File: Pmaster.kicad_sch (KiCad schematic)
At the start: 158 parts, among them U1 Pico, U2 Pico, U3 LM4040LP-3, U4 Pico, U5 Pico

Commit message: First try to fit electronic on PCB
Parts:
- NT294: renamed from NT291; symbol Device:NetTie_2 -> Analog_ADC:INA219AxDCN
- R15: renamed from R24; symbol Device:R_US -> Analog_ADC:INA219AxDCN
- TP26: renamed from TP29; footprint Connector_Pin:Pin_D1.2mm_L11.3mm_W3.0mm_Flat -> Connector_Pin:Pin_D1.0mm_L10.0mm
- TP27: renamed from TP30; footprint Connector_Pin:Pin_D1.2mm_L11.3mm_W3.0mm_Flat -> Connector_Pin:Pin_D1.0mm_L10.0mm
- TP28: renamed from TP31; footprint Connector_Pin:Pin_D1.2mm_L11.3mm_W3.0mm_Flat -> Connector_Pin:Pin_D1.0mm_L10.0mm
- TP29: renamed from TP32; footprint Connector_Pin:Pin_D1.2mm_L11.3mm_W3.0mm_Flat -> Connector_Pin:Pin_D1.0mm_L10.0mm
- TP30: renamed from TP33; footprint Connector_Pin:Pin_D1.2mm_L11.3mm_W3.0mm_Flat -> Connector_Pin:Pin_D1.0mm_L10.0mm
- TP31: renamed from TP34; footprint Connector_Pin:Pin_D1.2mm_L11.3mm_W3.0mm_Flat -> Connector_Pin:Pin_D1.0mm_L10.0mm
- TP32: renamed from TP35; footprint Connector_Pin:Pin_D1.2mm_L11.3mm_W3.0mm_Flat -> Connector_Pin:Pin_D1.0mm_L10.0mm
- TP33: renamed from TP36; footprint Connector_Pin:Pin_D1.2mm_L11.3mm_W3.0mm_Flat -> Connector_Pin:Pin_D1.0mm_L10.0mm
- TP34: renamed from TP37; footprint Connector_Pin:Pin_D1.2mm_L11.3mm_W3.0mm_Flat -> Connector_Pin:Pin_D1.0mm_L10.0mm
- TP35: renamed from TP38; footprint Connector_Pin:Pin_D1.2mm_L11.3mm_W3.0mm_Flat -> Connector_Pin:Pin_D1.0mm_L10.0mm
- TP36: renamed from TP39; footprint Connector_Pin:Pin_D1.2mm_L11.3mm_W3.0mm_Flat -> Connector_Pin:Pin_D1.0mm_L10.0mm
- TP37: renamed from TP40; footprint Connector_Pin:Pin_D1.2mm_L11.3mm_W3.0mm_Flat -> Connector_Pin:Pin_D1.0mm_L10.0mm
- TP38: renamed from TP41; footprint Connector_Pin:Pin_D1.2mm_L11.3mm_W3.0mm_Flat -> Connector_Pin:Pin_D1.0mm_L10.0mm
- TP39: renamed from TP42; footprint Connector_Pin:Pin_D1.2mm_L11.3mm_W3.0mm_Flat -> Connector_Pin:Pin_D1.0mm_L10.0mm
- TP40: renamed from TP43; footprint Connector_Pin:Pin_D1.2mm_L11.3mm_W3.0mm_Flat -> Connector_Pin:Pin_D1.0mm_L10.0mm
- TP41: renamed from TP44; footprint Connector_Pin:Pin_D1.2mm_L11.3mm_W3.0mm_Flat -> Connector_Pin:Pin_D1.0mm_L10.0mm
- TP42: renamed from TP45; footprint Connector_Pin:Pin_D1.2mm_L11.3mm_W3.0mm_Flat -> Connector_Pin:Pin_D1.0mm_L10.0mm
- TP43: renamed from TP46; footprint Connector_Pin:Pin_D1.2mm_L11.3mm_W3.0mm_Flat -> Connector_Pin:Pin_D1.0mm_L10.0mm
- TP44: renamed from TP47; footprint Connector_Pin:Pin_D1.2mm_L11.3mm_W3.0mm_Flat -> Connector_Pin:Pin_D1.0mm_L10.0mm
- TP45: renamed from TP48; footprint Connector_Pin:Pin_D1.2mm_L11.3mm_W3.0mm_Flat -> Connector_Pin:Pin_D1.0mm_L10.0mm
- TP46: renamed from TP49; footprint Connector_Pin:Pin_D1.2mm_L11.3mm_W3.0mm_Flat -> Connector_Pin:Pin_D1.0mm_L10.0mm
- TP47: renamed from TP50; footprint Connector_Pin:Pin_D1.2mm_L11.3mm_W3.0mm_Flat -> Connector_Pin:Pin_D1.0mm_L10.0mm
- TP48: renamed from TP51; footprint Connector_Pin:Pin_D1.2mm_L11.3mm_W3.0mm_Flat -> Connector_Pin:Pin_D1.0mm_L10.0mm
- TP49: renamed from TP52; footprint Connector_Pin:Pin_D1.2mm_L11.3mm_W3.0mm_Flat -> Connector_Pin:Pin_D1.0mm_L10.0mm
- TP50: renamed from TP53; footprint Connector_Pin:Pin_D1.2mm_L11.3mm_W3.0mm_Flat -> Connector_Pin:Pin_D1.0mm_L10.0mm
- TP51: renamed from TP54; footprint Connector_Pin:Pin_D1.2mm_L11.3mm_W3.0mm_Flat -> Connector_Pin:Pin_D1.0mm_L10.0mm
- TP52: renamed from TP55; footprint Connector_Pin:Pin_D1.2mm_L11.3mm_W3.0mm_Flat -> Connector_Pin:Pin_D1.0mm_L10.0mm
- TP53: renamed from TP56; footprint Connector_Pin:Pin_D1.2mm_L11.3mm_W3.0mm_Flat -> Connector_Pin:Pin_D1.0mm_L10.0mm
- TP54: renamed from TP57; footprint Connector_Pin:Pin_D1.2mm_L11.3mm_W3.0mm_Flat -> Connector_Pin:Pin_D1.0mm_L10.0mm
- renumbered NT230 to NT233, NT231 to NT234, NT232 to NT235, NT233 to NT236, NT234 to NT237, NT235 to NT238, NT236 to NT239, NT237 to NT240, NT238 to NT241, NT239 to NT242, NT240 to NT243, NT241 to NT244, NT242 to NT245, NT243 to NT246, NT244 to NT247, NT245 to NT248, NT246 to NT249, NT247 to NT250, NT248 to NT251, NT249 to NT252, NT250 to NT253, NT251 to NT254, NT252 to NT255, NT253 to NT256, NT254 to NT257, NT255 to NT258, NT256 to NT259, NT257 to NT260, NT258 to NT261, NT259 to NT262, NT260 to NT263, NT261 to NT264, NT262 to NT265, NT263 to NT266, NT264 to NT267, NT265 to NT268, NT266 to NT269, NT267 to NT270, NT268 to NT271, NT269 to NT272, NT270 to NT273, NT271 to NT274, NT272 to NT275, NT273 to NT276, NT274 to NT277, NT275 to NT278, NT276 to NT279, NT277 to NT280, NT278 to NT281, NT279 to NT282, NT280 to NT283, NT281 to NT284, NT282 to NT285, NT283 to NT286, NT284 to NT287, NT285 to NT288, NT286 to NT289, NT287 to NT290, NT288 to NT291, NT289 to NT292, NT290 to NT293, NT292 to NT295, NT293 to NT296, NT294 to NT297, NT295 to NT298, NT296 to NT299, NT297 to NT300, NT298 to NT301, NT299 to NT302, NT300 to NT303, NT301 to NT304, NT302 to NT305, NT303 to NT306, NT304 to NT307, NT305 to NT308, NT306 to NT309, NT307 to NT310, NT308 to NT311, NT309 to NT312, NT310 to NT313, NT311 to NT314, NT312 to NT315, NT313 to NT316, NT314 to NT317, NT315 to NT318, NT316 to NT319, NT317 to NT320, NT318 to NT321, NT319 to NT322, NT320 to NT323, NT321 to NT324, NT322 to NT325, NT323 to NT326, NT324 to NT327, NT325 to NT328, NT326 to NT329, NT327 to NT330, NT328 to NT331, NT329 to NT332, NT330 to NT333, NT331 to NT334, NT332 to NT335, NT333 to NT336, NT334 to NT337, NT335 to NT338, NT336 to NT339, NT337 to NT340, NT338 to NT341, NT339 to NT342, NT340 to NT343, NT341 to NT344, NT342 to NT345, NT343 to NT346, NT344 to NT347, NT345 to NT348, R19 to R10, R20 to R11, R21 to R12, R22 to R13, R23 to R14, R25 to R16, R26 to R17, U4 to U3, U5 to U4, U3 to U5
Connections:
- net B31_D: no longer NT294.1
- net GND: no longer R15.1
- net S2_I2C_ID1: no longer R15.2
- net at U4.2 (GPIO1): no longer NT294.2

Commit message: backup 1 bank done
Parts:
- removed NT294: S3_01, NetTie:NetTie-2_THT_Pad1.0mm, symbol Analog_ADC:INA219AxDCN
- removed R15: 4.7K, Resistor_THT:R_Axial_DIN0309_L9.0mm_D3.2mm_P12.70mm_Horizontal, symbol Analog_ADC:INA219AxDCN
- added NT294: S3_01, NetTie:NetTie-2_Front1.0mm, symbol Device:NetTie_2
- added R1: 4.7K, Resistor_THT:R_Axial_DIN0309_L9.0mm_D3.2mm_P12.70mm_Horizontal, symbol Device:R_US
- NT233, NT234, NT235, NT236, NT237, NT238, NT239, NT240, NT241, NT242, NT243, NT244, NT245, NT246, NT247, NT248, NT249, NT250, NT251, NT252, NT253, NT254, NT255, NT256, NT257, NT258, NT259, NT260, NT261, NT262, NT263, NT264, NT265, NT266, NT267, NT268, NT269, NT270, NT271, NT272, NT273, NT274, NT275, NT276, NT277, NT278, NT279, NT280, NT281, NT282, NT283, NT284, NT285, NT286, NT287, NT288, NT289, NT290, NT291, NT292, NT293, NT295, NT296, NT297, NT298, NT299, NT300, NT301, NT302, NT303, NT304, NT305, NT306, NT307, NT308, NT309, NT310, NT311, NT312, NT313, NT314, NT315, NT316, NT317, NT318, NT319, NT320, NT321, NT322, NT323, NT324, NT325, NT326, NT327, NT328, NT329, NT330, NT331, NT332, NT333, NT334, NT335, NT336, NT337, NT338, NT339, NT340, NT341, NT342, NT343, NT344, NT345, NT346, NT347, NT348: footprint NetTie:NetTie-2_THT_Pad1.0mm -> NetTie:NetTie-2_Front1.0mm
- TP26, TP27, TP28, TP29, TP30, TP31, TP32, TP33, TP34, TP35, TP36, TP37, TP38, TP39, TP40, TP41, TP42, TP43, TP44, TP45, TP46, TP47, TP48, TP49, TP50, TP51, TP52, TP53, TP54: footprint Connector_Pin:Pin_D1.0mm_L10.0mm -> Connector_Pin:Pin_D0.9mm_L10.0mm_W2.4mm_FlatFork
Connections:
- net B31_D: now also NT294.1
- net GND: now also R1.1
- net S2_I2C_ID1: now also R1.2
- net at U4.2 (GPIO1): now also NT294.2

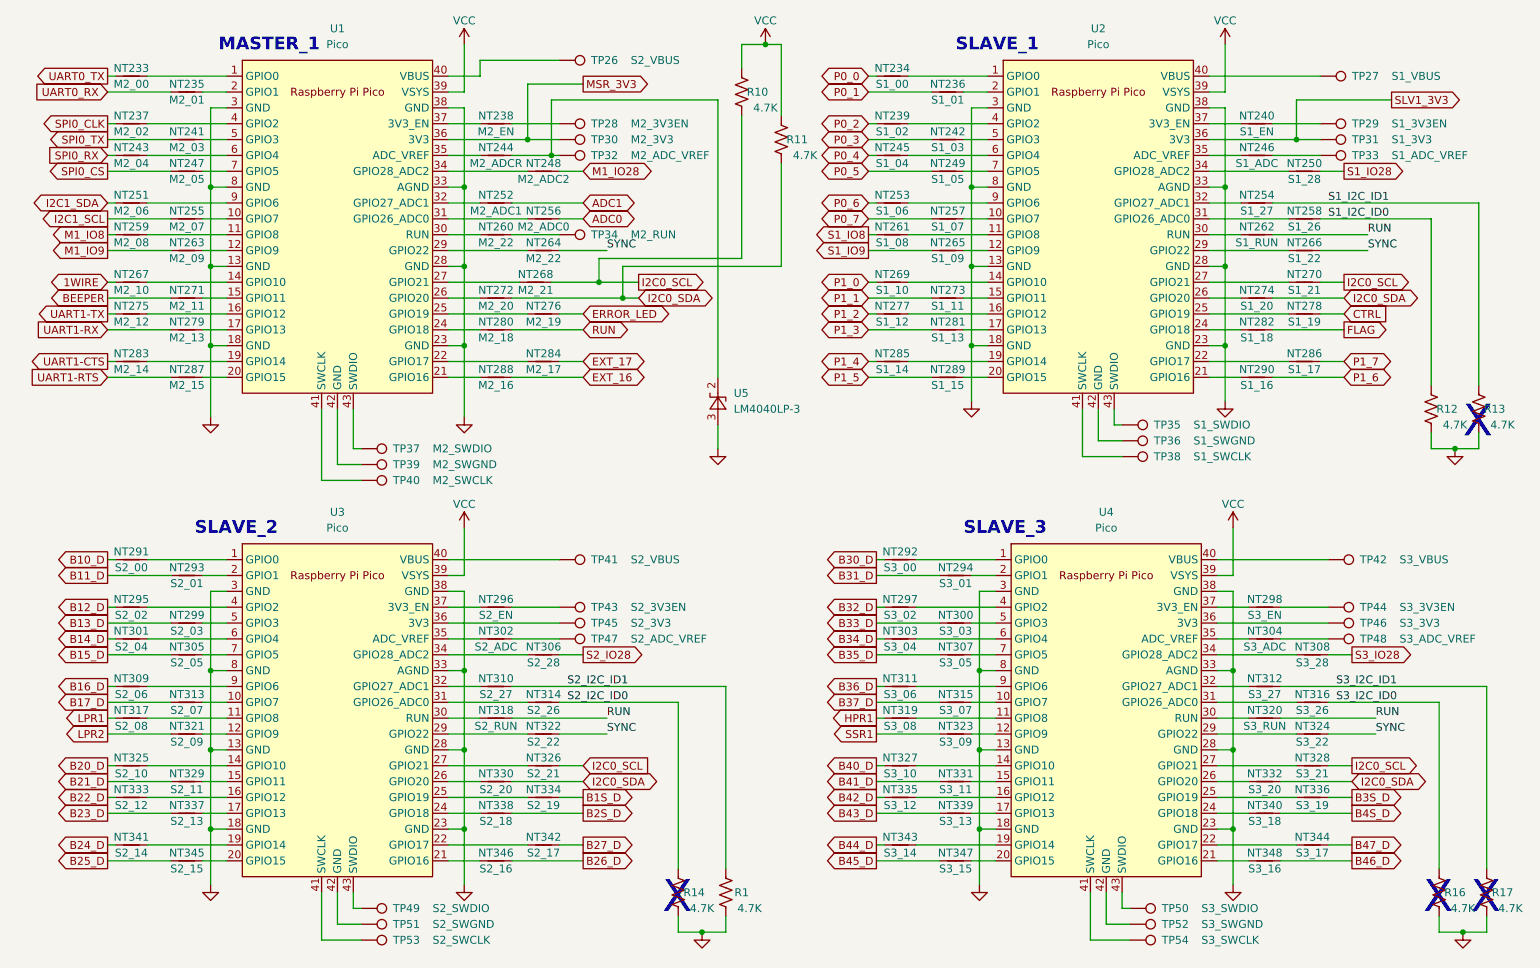
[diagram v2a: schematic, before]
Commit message: half PCB completed
FTS io controller PCB
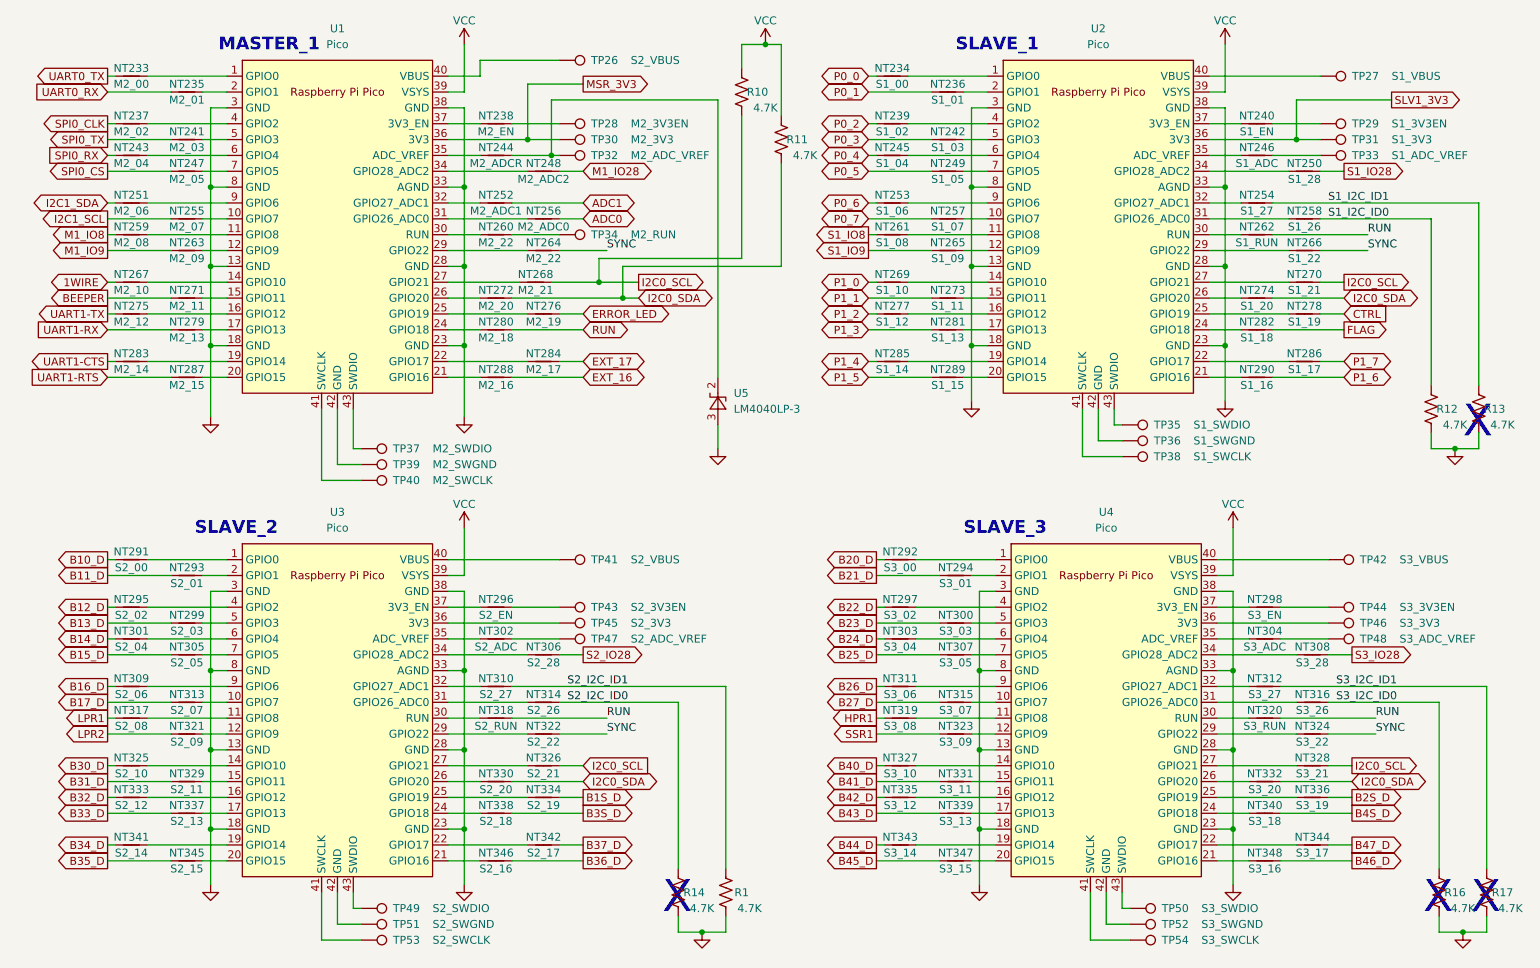
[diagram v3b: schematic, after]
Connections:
- net B20_D: now also NT292.1; no longer NT325.1
- net B21_D: now also NT294.1; no longer NT329.1
- net B22_D: now also NT297.1; no longer NT333.1
- net B23_D: now also NT300.1; no longer NT337.1
- net B24_D: now also NT303.1; no longer NT341.1
- net B25_D: now also NT307.1; no longer NT345.1
- net B26_D: now also NT311.1; no longer NT346.1
- net B27_D: now also NT315.1; no longer NT342.1
- net B2S_D: now also NT336.1; no longer NT338.1
- net B30_D: now also NT325.1; no longer NT292.1
- net B31_D: now also NT329.1; no longer NT294.1
- net B32_D: now also NT333.1; no longer NT297.1
- net B33_D: now also NT337.1; no longer NT300.1
- net B34_D: now also NT341.1; no longer NT303.1
- net B35_D: now also NT345.1; no longer NT307.1
- net B36_D: now also NT346.1; no longer NT311.1
- net B37_D: now also NT342.1; no longer NT315.1
- net B3S_D: now also NT338.1; no longer NT336.1
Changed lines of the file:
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@@
     )
   )
-  (global_label "B36_D" (shape output) (at 149.86 121.92 180) (fields_autoplaced)
+  (global_label "B26_D" (shape output) (at 149.86 121.92 180) (fields_autoplaced)
     (effects (font (size 1.27 1.27)) (justify right))
     (property "Intersheet References" "${INTERSHEET_REFS}" (id 0) (at 141.5202 121.8406 0)
@@
     )
   )
-  (global_label "B33_D" (shape output) (at 149.86 111.76 180) (fields_autoplaced)
+  (global_label "B23_D" (shape output) (at 149.86 111.76 180) (fields_autoplaced)
     (effects (font (size 1.27 1.27)) (justify right))
     (property "Intersheet References" "${INTERSHEET_REFS}" (id 0) (at 141.5202 111.6806 0)
@@
     )
   )
-  (global_label "B2S_D" (shape output) (at 102.87 142.24 0) (fields_autoplaced)
+  (global_label "B3S_D" (shape output) (at 102.87 142.24 0) (fields_autoplaced)
     (effects (font (size 1.27 1.27)) (justify left))
     (property "Intersheet References" "${INTERSHEET_REFS}" (id 0) (at 111.2098 142.1606 0)
@@
     )
   )
-  (global_label "B35_D" (shape output) (at 149.86 116.84 180) (fields_autoplaced)
+  (global_label "B25_D" (shape output) (at 149.86 116.84 180) (fields_autoplaced)
     (effects (font (size 1.27 1.27)) (justify right))
     (property "Intersheet References" "${INTERSHEET_REFS}" (id 0) (at 141.5202 116.7606 0)
@@
     )
   )
-  (global_label "B34_D" (shape output) (at 149.86 114.3 180) (fields_autoplaced)
+  (global_label "B24_D" (shape output) (at 149.86 114.3 180) (fields_autoplaced)
     (effects (font (size 1.27 1.27)) (justify right))
     (property "Intersheet References" "${INTERSHEET_REFS}" (id 0) (at 141.5202 114.2206 0)
@@
     )
   )
-  (global_label "B24_D" (shape output) (at 26.67 147.32 180) (fields_autoplaced)
+  (global_label "B34_D" (shape output) (at 26.67 147.32 180) (fields_autoplaced)
     (effects (font (size 1.27 1.27)) (justify right))
     (property "Intersheet References" "${INTERSHEET_REFS}" (id 0) (at 18.3302 147.2406 0)
@@
     )
   )
-  (global_label "B27_D" (shape output) (at 102.87 147.32 0) (fields_autoplaced)
+  (global_label "B37_D" (shape output) (at 102.87 147.32 0) (fields_autoplaced)
     (effects (font (size 1.27 1.27)) (justify left))
     (property "Intersheet References" "${INTERSHEET_REFS}" (id 0) (at 111.2098 147.2406 0)
@@
     )
   )
-  (global_label "B21_D" (shape output) (at 26.67 137.16 180) (fields_autoplaced)
+  (global_label "B31_D" (shape output) (at 26.67 137.16 180) (fields_autoplaced)
     (effects (font (size 1.27 1.27)) (justify right))
     (property "Intersheet References" "${INTERSHEET_REFS}" (id 0) (at 18.3302 137.0806 0)
@@
     )
   )
-  (global_label "B3S_D" (shape output) (at 226.06 139.7 0) (fields_autoplaced)
+  (global_label "B2S_D" (shape output) (at 226.06 139.7 0) (fields_autoplaced)
     (effects (font (size 1.27 1.27)) (justify left))
     (property "Intersheet References" "${INTERSHEET_REFS}" (id 0) (at 234.3998 139.6206 0)
@@
     )
   )
-  (global_label "B22_D" (shape output) (at 26.67 139.7 180) (fields_autoplaced)
+  (global_label "B32_D" (shape output) (at 26.67 139.7 180) (fields_autoplaced)
     (effects (font (size 1.27 1.27)) (justify right))
     (property "Intersheet References" "${INTERSHEET_REFS}" (id 0) (at 18.3302 139.6206 0)
@@
     )
   )
-  (global_label "B23_D" (shape output) (at 26.67 142.24 180) (fields_autoplaced)
+  (global_label "B33_D" (shape output) (at 26.67 142.24 180) (fields_autoplaced)
     (effects (font (size 1.27 1.27)) (justify right))
     (property "Intersheet References" "${INTERSHEET_REFS}" (id 0) (at 18.3302 142.1606 0)
@@
     )
   )
-  (global_label "B20_D" (shape output) (at 26.67 134.62 180) (fields_autoplaced)
+  (global_label "B30_D" (shape output) (at 26.67 134.62 180) (fields_autoplaced)
     (effects (font (size 1.27 1.27)) (justify right))
     (property "Intersheet References" "${INTERSHEET_REFS}" (id 0) (at 18.3302 134.5406 0)
@@
     )
   )
-  (global_label "B32_D" (shape output) (at 149.86 109.22 180) (fields_autoplaced)
+  (global_label "B22_D" (shape output) (at 149.86 109.22 180) (fields_autoplaced)
     (effects (font (size 1.27 1.27)) (justify right))
     (property "Intersheet References" "${INTERSHEET_REFS}" (id 0) (at 141.5202 109.1406 0)
@@
     )
   )
-  (global_label "B37_D" (shape output) (at 149.86 124.46 180) (fields_autoplaced)
+  (global_label "B27_D" (shape output) (at 149.86 124.46 180) (fields_autoplaced)
     (effects (font (size 1.27 1.27)) (justify right))
     (property "Intersheet References" "${INTERSHEET_REFS}" (id 0) (at 141.5202 124.3806 0)
@@
     )
   )
-  (global_label "B26_D" (shape output) (at 102.87 149.86 0) (fields_autoplaced)
+  (global_label "B36_D" (shape output) (at 102.87 149.86 0) (fields_autoplaced)
     (effects (font (size 1.27 1.27)) (justify left))
     (property "Intersheet References" "${INTERSHEET_REFS}" (id 0) (at 111.2098 149.7806 0)
@@
     )
   )
-  (global_label "B25_D" (shape output) (at 26.67 149.86 180) (fields_autoplaced)
+  (global_label "B35_D" (shape output) (at 26.67 149.86 180) (fields_autoplaced)
     (effects (font (size 1.27 1.27)) (justify right))
     (property "Intersheet References" "${INTERSHEET_REFS}" (id 0) (at 18.3302 149.7806 0)
@@
     )
   )
-  (global_label "B31_D" (shape output) (at 149.86 104.14 180) (fields_autoplaced)
+  (global_label "B21_D" (shape output) (at 149.86 104.14 180) (fields_autoplaced)
     (effects (font (size 1.27 1.27)) (justify right))
     (property "Intersheet References" "${INTERSHEET_REFS}" (id 0) (at 141.5202 104.0606 0)
@@
     )
   )
-  (global_label "B30_D" (shape output) (at 149.86 101.6 180) (fields_autoplaced)
+  (global_label "B20_D" (shape output) (at 149.86 101.6 180) (fields_autoplaced)
     (effects (font (size 1.27 1.27)) (justify right))
     (property "Intersheet References" "${INTERSHEET_REFS}" (id 0) (at 141.5202 101.5206 0)

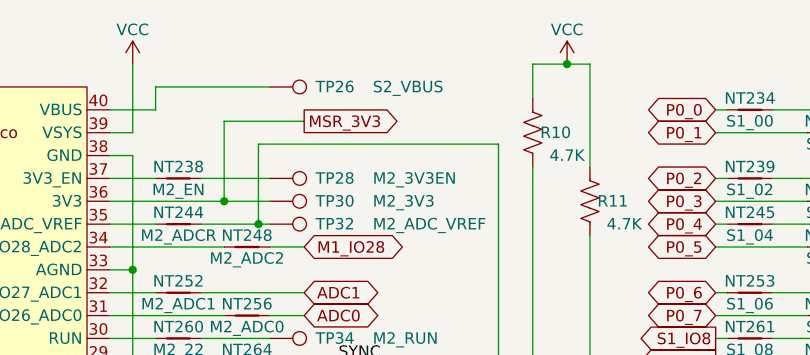
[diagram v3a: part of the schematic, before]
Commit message: PCB Completed
PCB completed but final verification not completed
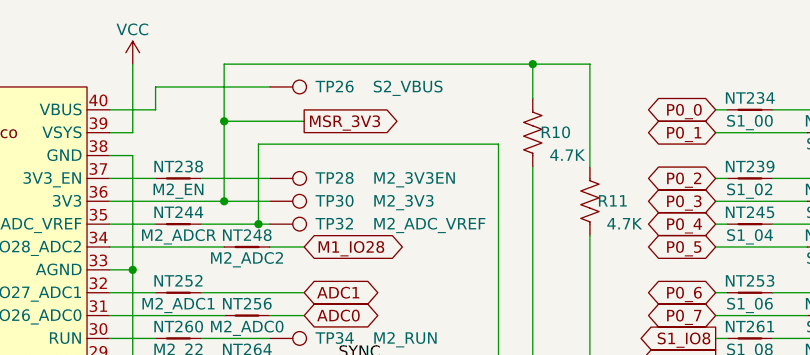
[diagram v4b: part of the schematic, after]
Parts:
- TP26, TP27, TP28, TP29, TP30, TP31, TP32, TP33, TP34, TP35, TP36, TP37, TP38, TP39, TP40, TP41, TP42, TP43, TP44, TP45, TP46, TP47, TP48, TP49, TP50, TP51, TP52, TP53, TP54: footprint Connector_Pin:Pin_D0.9mm_L10.0mm_W2.4mm_FlatFork -> TestPoint:TestPoint_THTPad_D1.5mm_Drill0.7mm
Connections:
- net MSR_3V3: now also R10.2, R11.2
- net VCC: no longer R10.2, R11.2

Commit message: update
Correction of small error
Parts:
- NT244: value M2_ADCR -> AGND
- R1, R10, R11, R12, R13, R14, R16, R17: footprint Resistor_THT:R_Axial_DIN0309_L9.0mm_D3.2mm_P12.70mm_Horizontal -> Resistor_THT:R_Axial_DIN0207_L6.3mm_D2.5mm_P10.16mm_Horizontal
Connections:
- net GND: now also NT244.2; no longer U1.33 (AGND), U5.3 (A)
- net at TP32.1, U5.2 (K): now also U1.35 (ADC_VREF); no longer NT244.2
- net at NT244.1: now also U1.33 (AGND), U5.3 (A); no longer U1.35 (ADC_VREF)
- net M1_IO28 renamed OE
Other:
- moved on the sheet: NT248, U5
